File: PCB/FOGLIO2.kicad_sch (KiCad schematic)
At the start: 56 parts, among them U11 OPA4350EA_250, U12 OPA4350EA_250, U13 OPA4350EA_250, U6 OPA4350EA_250

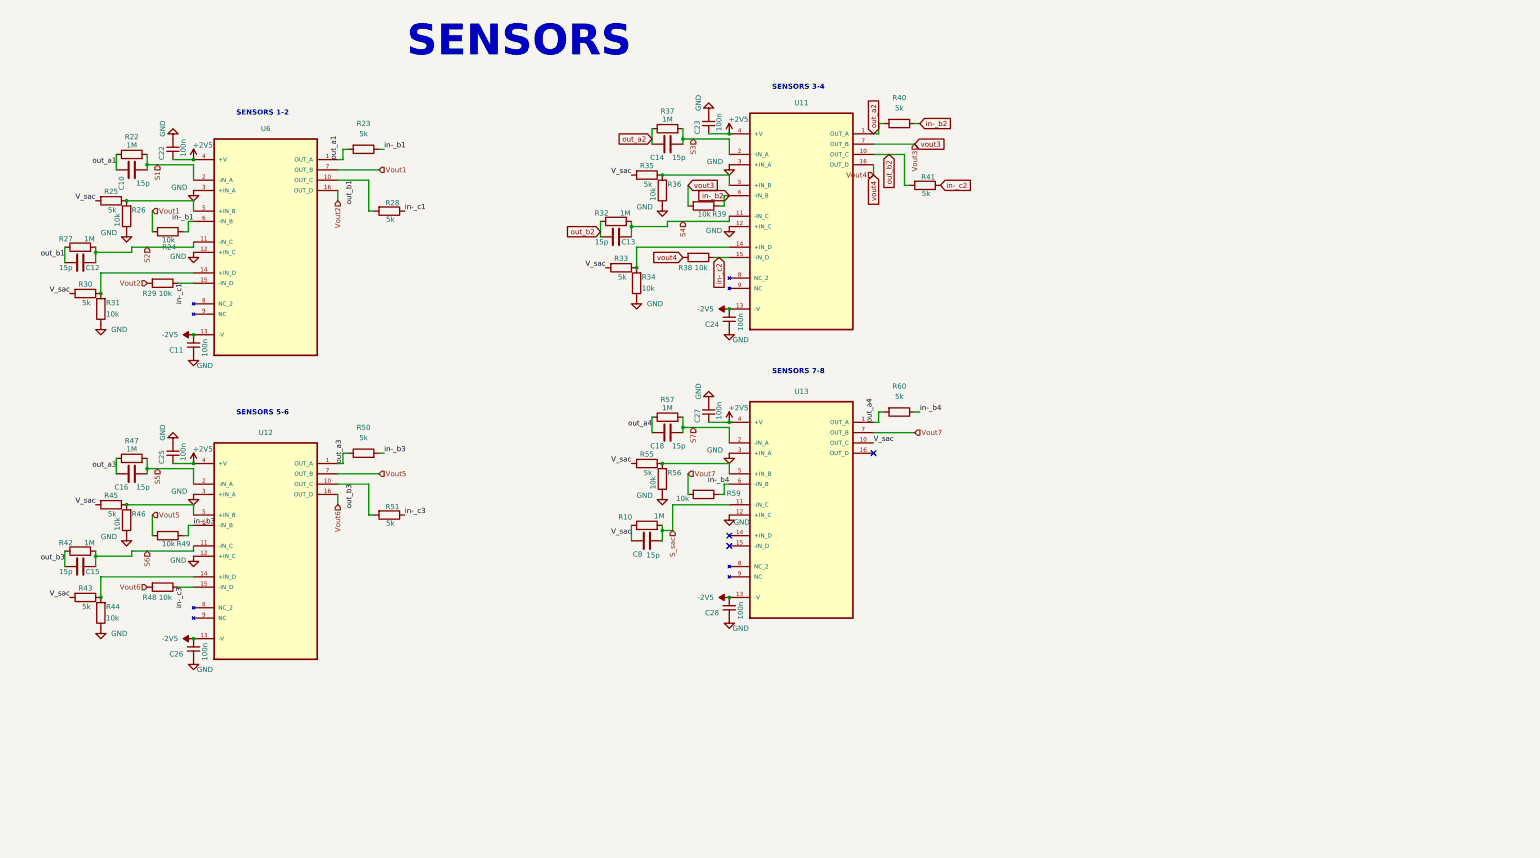
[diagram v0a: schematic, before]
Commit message: Swap AD7606 for ADS131M08, rework analog front-end and USB input
Schematic-only changes; the PCB has not been updated from the schematic
yet. PCB/CHANGELOG-2026-09-28-ADC-swap.md has the per-part details: every
added/removed part with its pin-to-net list, the netlist diff (before ->
after) and the ERC counts.

1. ADC swap (FOGLIO1)
- Remove the AD7606 (U5) and parts that only served it: C29-C32, C45-C47,
  BUSY LED D3/R8 and the old 1x07 J7.
- Wire up the ADS131M08 (U2): internal 1.2 V reference with 100n on REFIN,
  XTAL2 no-connect, AINxN tied to GND.
- Per-channel divider + anti-alias RC (R61-R76 1.1k/1k, C48-C55 10n C0G):
  op-amp swing +-2.45 V -> +-1.17 V for the +-1.2 V ADC full scale,
  fc ~30 kHz. Channel 7 now digitises the sacrificial-sensor output Vsac.
- ADC supply: U7 TPS7A2033 LDO from +5V -> +3.3VA (AVDD), FB1 -> +3V3
  (DVDD, U3, pull-ups). 1.7 V headroom gives full PSRR, which a passive
  filter on raw VBUS could not.
- Clock from the STM32H7 (MCO2, 5.12 MHz, OSR 256 -> 10 kSPS):
  MCU_CLK -> U3 74LVC1G17 Schmitt buffer -> R80 33R -> CLKIN, with R79
  100k pull-down so CLKIN never floats.
- SPI: R81/R82 33R source terminations on DOUT/DRDY, R77/R78 10k pull-ups
  on CS and SYNC/RESET.
- New 2x06 J7 with GND next to CLK and SCLK.
- Vsac brought from the SENSORS sheet through a new sheet pin (plain wire
  on the root sheet).
- FOGLIO1 paper A4 -> A3. PWR_FLAG added on GND (pre-existing ERC error).

2. Op-amp section swap (FOGLIO2)
- U6 and U13, the two quads next to J3, now hold all 8 first stages
  (S1-S7 and S_sac); U11/U12 hold the 7 difference amps. The
  high-impedance sensor traces can now stay short and on F.Cu.
- Section order chosen from the J3/op-amp pad positions so the sensor
  traces can be routed without crossings.
- Spare section U12-D wired as a follower with +IN at GND (previously
  U13-D was left floating).
- Passive references, values and symbol UUIDs are unchanged, so the PCB
  footprints stay linked.

3. SENSORS sheet readability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
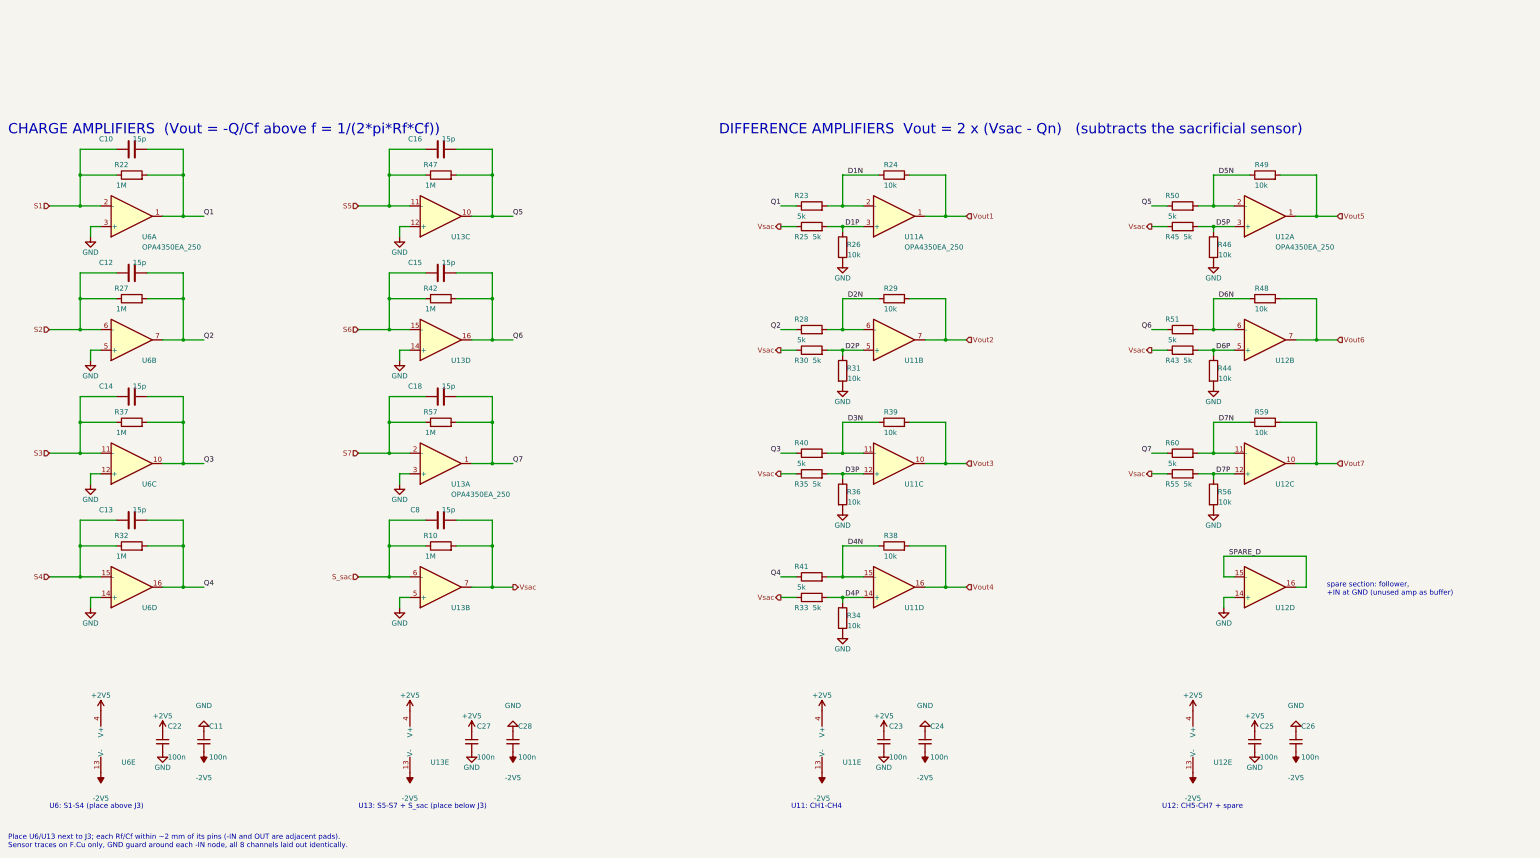
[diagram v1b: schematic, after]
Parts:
- added unit 2 of U11
- added unit 4 of U11
- added unit 3 of U11
- added unit 5 of U11
- added unit 4 of U12
- added unit 5 of U12
- added unit 2 of U12
- added unit 3 of U12
- added unit 4 of U13
- added unit 5 of U13
- added unit 2 of U13
- added unit 3 of U13
- added unit 5 of U6
- added unit 3 of U6
- added unit 4 of U6
- added unit 2 of U6
- U11, U12, U13, U6: symbol OPA4350EA_250:OPA4350EA_250 -> Amplifier_Operational:OPA4340EA
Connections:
- net +2V5: now also U11.4 (V+), U12.4 (V+), U13.4 (V+), U6.4 (V+); no longer U11.4 (+V), U12.4 (+V), U13.4 (+V), U6.4 (+V)
- net -2V5: now also U11.13 (V-), U12.13 (V-), U13.13 (V-), U6.13 (V-); no longer U11.13 (-V), U12.13 (-V), U13.13 (-V), U6.13 (-V)
- net GND: now also R26.2, R31.2, R34.2, R36.2, R44.2, R46.2, R56.2, U12.14 (+), U13.12 (+), U13.14 (+), U13.5 (+), U6.12 (+), U6.14 (+), U6.5 (+); no longer R26.1, R31.1, R34.1, R36.1, R44.1, R46.1, R56.1, U11.12 (+IN_C), U11.3 (+IN_A), U12.12 (+IN_C), U12.3 (+IN_A), U13.12 (+IN_C), U6.12 (+IN_C)
- net S1: now also C10.1, R22.1; no longer C10.2, R22.2
- net S2: now also C12.1, R27.1, U6.6 (-); no longer C12.2, R27.2, U6.11 (-IN_C)
- net S3: now also C14.1, R37.1, U6.11 (-); no longer C14.2, R37.2, U11.2 (-IN_A)
- net S4: now also C13.1, R32.1, U6.15 (-); no longer C13.2, R32.2, U11.11 (-IN_C)
- net S5: now also C16.1, R47.1, U13.11 (-); no longer C16.2, R47.2, U12.2 (-IN_A)
- net S6: now also C15.1, R42.1, U13.15 (-); no longer C15.2, R42.2, U12.11 (-IN_C)
- net S7: now also C18.1, R57.1; no longer C18.2, R57.2
- net S_sac: now also C8.1, R10.1, U13.6 (-); no longer C8.2, R10.2, U13.11 (-IN_C)
- net Vout1: now also U11.1; no longer U6.7 (OUT_B)
- net Vout2: now also U11.7; no longer U6.16 (OUT_D)
- net Vout5: now also U12.1; no longer U12.7 (OUT_B)
- net Vout6: now also U12.7; no longer U12.16 (OUT_D)
- net Vout7: now also U12.10; no longer U13.7 (OUT_B)
- removed net V_sac: C8.1, R10.1, R25.2, R30.2, R33.2, R35.2, R43.2, R45.2, R55.2, U13.10 (OUT_C)
- removed net in-_b1: R23.1, R24.1, U6.6 (-IN_B)
- removed net in-_b2: R39.1, R40.1, U11.6 (-IN_B)
- net in-_b3 renamed D5N
- net D5N: now also U12.2 (-); no longer U12.6 (-IN_B)
- removed net in-_b4: R59.1, R60.1, U13.6 (-IN_B)
- removed net in-_c1: R28.1, R29.1, U6.15 (-IN_D)
- removed net in-_c2: R38.1, R41.1, U11.15 (-IN_D)
- removed net in-_c3: R48.1, R51.1, U12.15 (-IN_D)
- removed net out_a1: C10.1, R22.1, R23.2, U6.1 (OUT_A)
- removed net out_a2: C14.1, R37.1, R40.2, U11.1 (OUT_A)
- removed net out_a3: C16.1, R47.1, R50.1, U12.1 (OUT_A)
- removed net out_a4: C18.1, R57.1, R60.2, U13.1 (OUT_A)
- removed net out_b1: C12.1, R27.1, R28.2, U6.10 (OUT_C)
- removed net out_b2: C13.1, R32.1, R41.2, U11.10 (OUT_C)
- removed net out_b3: C15.1, R42.1, R51.2, U12.10 (OUT_C)
- net vout3 renamed Vout3
- net Vout3: now also U11.10; no longer U11.7 (OUT_B)
- net vout4 renamed Vout4
- net Vout4: now also U11.16; no longer U11.16 (OUT_D)
- new net D1N: R23.2, R24.1, U11.2 (-)
- new net D1P: R25.2, R26.1, U11.3 (+)
- new net D2N: R28.2, R29.1, U11.6 (-)
- new net D2P: R30.2, R31.1, U11.5 (+)
- new net D3N: R39.1, R40.2, U11.11 (-)
- new net D3P: R35.2, R36.1, U11.12 (+)
- new net D4N: R38.1, R41.2, U11.15 (-)
- new net D4P: R33.2, R34.1, U11.14 (+)
- new net D5P: R45.2, R46.1, U12.3 (+)
- new net D6N: R48.1, R51.2, U12.6 (-)
- new net D6P: R43.2, R44.1, U12.5 (+)
- new net D7N: R59.1, R60.2, U12.11 (-)
- new net D7P: R55.2, R56.1, U12.12 (+)
- new net Q1: C10.2, R22.2, R23.1, U6.1
- new net Q2: C12.2, R27.2, R28.1, U6.7
- new net Q3: C14.2, R37.2, R40.1, U6.10
- new net Q4: C13.2, R32.2, R41.1, U6.16
- new net Q5: C16.2, R47.2, R50.1, U13.10
- new net Q6: C15.2, R42.2, R51.1, U13.16
- new net Q7: C18.2, R57.2, R60.1, U13.1
- new net SPARE_D: U12.15 (-), U12.16
- new net Vsac: C8.2, R10.2, R25.1, R30.1, R33.1, R35.1, R43.1, R45.1, R55.1, U13.7
- no-connect marks 3 -> 0
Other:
- note added: "CHARGE AMPLIFIERS (Vout = -Q/Cf above f = 1/(2*pi*Rf*Cf))"
- note added: "DIFFERENCE AMPLIFIERS Vout = 2 x (Vsac - Qn) (subtracts the sacrificial sensor)"
- note added: "Place U6/U13 next to J3; each Rf/Cf within ~2 mm of its pins (-IN and OUT are adjacent pads). Sensor traces on F.Cu only, GND guard around each -IN node, all 8 channels laid out identically."
- note added: "U11: CH1-CH4"
- note added: "U12: CH5-CH7 + spare"
- note added: "U13: S5-S7 + S_sac (place below J3)"
- note added: "U6: S1-S4 (place above J3)"
- note added: "spare section: follower, +IN at GND (unused amp as buffer)"
- note removed: "SENSORS"
- note removed: "SENSORS 1-2"
- note removed: "SENSORS 3-4"
- note removed: "SENSORS 5-6"
- note removed: "SENSORS 7-8"
- moved on the sheet: C10, C11, C12, C13, C14, C15, C16, C18, C22, C23, C24, C25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

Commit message: Add MPNs to all parts, switch unavailable parts, add Mouser BOM
Schematic procurement pass, based on a Mouser Italia stock/price check
(2026-09-28). The netlist is unchanged and ERC is still at 0 errors.
Details are in PCB/CHANGELOG-2026-09-28-ADC-swap.md, Part 5.

Schematic (FOGLIO1, FOGLIO2):
- Every orderable part (123) now has MPN and Manufacturer fields. The
  old SnapEDA "MF" field on the op-amps is replaced by Manufacturer.
- Difference-amp resistors 5k -> 4.99k (R23, R25, R28, R30, R33, R35,
  R40, R41, R43, R45, R50, R51, R55, R60). Exact 5.0k only exists at
  0.1 %/25 ppm for about EUR 1.7. Both halves of each difference amp use
  the same 4.99k/10k pair, so the ratio still matches (gain 2.004).
- U7 TPS7A2033PDBVR (out of stock, 26-week lead) -> LP5907MFX-3.3/NOPB.
  Same SOT-23-5 pinout and footprint (IN 1, GND 2, EN 3, NC 4, OUT 5).
  The symbol is now Regulator_Linear:LP5907MFX-3.3.
- C62 -> Murata GRM219R61C226ME15K, 22 uF 16 V X5R, footprint
  changed to 0805 (the 0603 ZRB part was out of stock until mid-October).
- Precision parts, all 0.1 % / 25 ppm thin film:
  - 1M Rf and 1k: KOA RN73R
  - 4.99k, 10k, 1.1k: Yageo RT0603BRD
- Capacitor MPNs:
  - 15 pF C0G: Samsung CL10C150JB8NNNC (all Murata 0603 parts are NRND)
  - 10 nF: GRM1885C1H103JA01D
  - 100 nF: GRM188R72A104KA35D (previous part obsolete)
  - 1 uF: GRT188R71E105KE13D (previous part obsolete)
  - 4.7 uF: GRT188R61C475KE13D (previous part not orderable)
  - 10 uF 0805: GRJ21BR61E106KE01L
  - 220 nF: GRM188R71E224KA88D
- General-purpose resistors: Yageo RC0603FR-07; 105k is
  AC0603FR-07105KL because the RC part has no stock.

BOM (PCB/bom/BOM_Mouser_2026-09-28.csv):
- 35 lines, 124 parts per board. Each line has quantity, references,
  value, description, manufacturer, MPN, Mouser link, stock and EUR
  price at qty 10/100.
- Priced parts come to about EUR 49 per board at qty 10.

Open points:
- J5 has no MPN yet (needs a 1x03 2.54 mm SMD alternating-pin header).
- Stock not checked for D2, J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
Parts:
- C10, C12, C13, C14, C15, C16, C18, C8: MPN (none) -> CL10C150JB8NNNC; Manufacturer (none) -> Samsung Electro-Mechanics
- C11, C22, C23, C24, C25, C26, C27, C28: MPN (none) -> GRM188R72A104KA35D; Manufacturer (none) -> Murata
- R10, R22, R27, R32, R37, R42, R47, R57: MPN (none) -> RN73R1JTTD1004B25; Manufacturer (none) -> KOA Speer
- R23, R25, R28, R30, R33, R35, R40, R41, R43, R45, R50, R51, R55, R60: value 5k -> 4.99k; MPN (none) -> RT0603BRD074K99L; Manufacturer (none) -> Yageo
- R24, R26, R29, R31, R34, R36, R38, R39, R44, R46, R48, R49, R56, R59: MPN (none) -> RT0603BRD0710KL; Manufacturer (none) -> Yageo
- U11, U12, U13, U6: MF Texas Instruments -> (none); Manufacturer (none) -> Texas Instruments
